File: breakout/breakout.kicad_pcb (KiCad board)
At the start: 2 copper layers, 20.3 x 22.9 mm, 6 parts, among them J1 Conn_01x02, J2 Conn_01x04, J3 Conn_01x05, J4 Conn_01x05, J5 Conn_01x03, U1 74HC4051

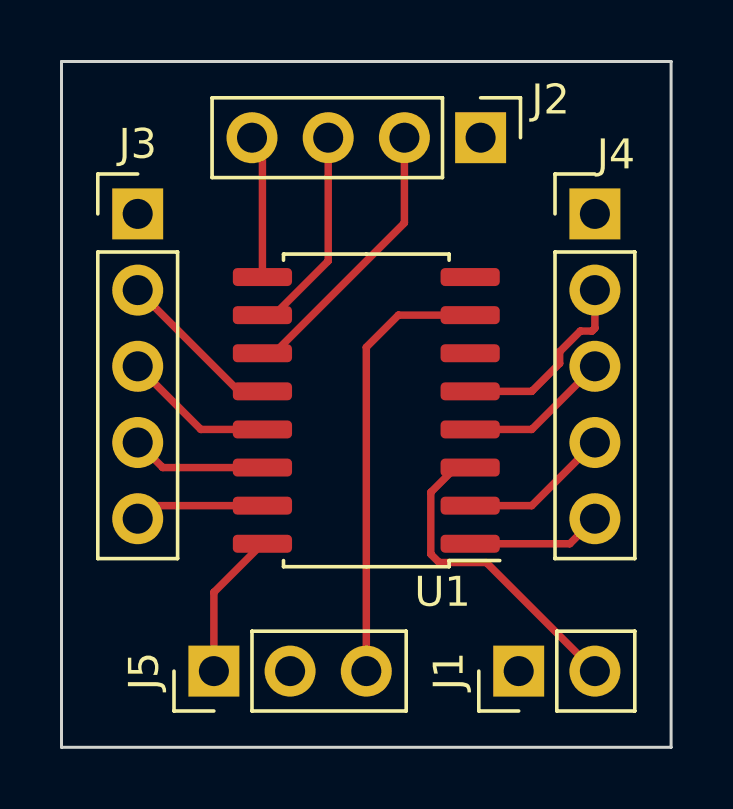
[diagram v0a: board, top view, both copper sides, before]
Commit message: Add 0805 decoupling capacitor pads to the breakout board.
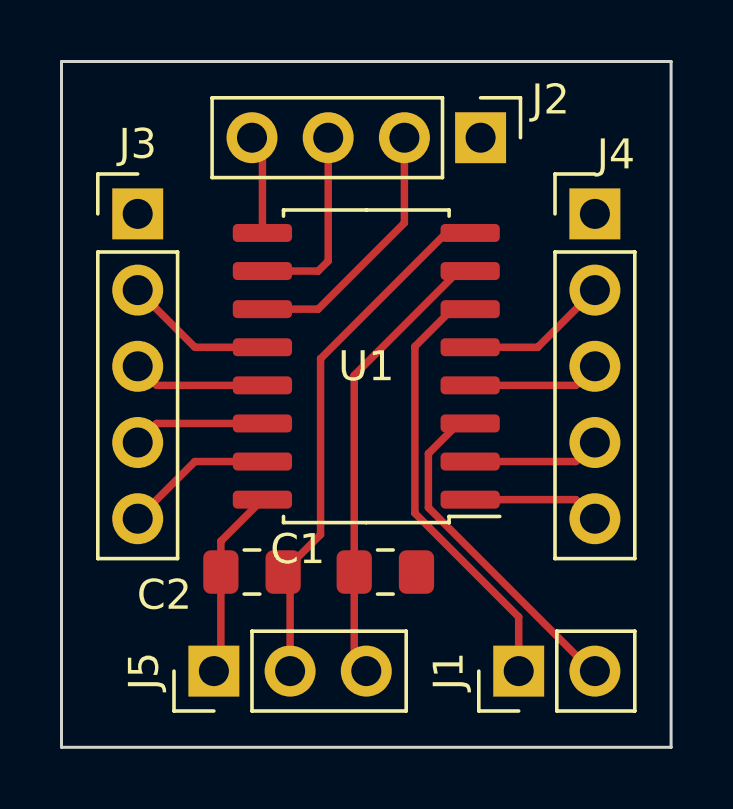
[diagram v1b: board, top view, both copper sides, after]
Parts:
- added C1: C, Capacitor_SMD:C_0805_2012Metric_Pad1.18x1.45mm_HandSolder, F.Cu at (130.2, 95.8)
- added C2: C, Capacitor_SMD:C_0805_2012Metric_Pad1.18x1.45mm_HandSolder, F.Cu at (125.7, 95.8)
- moved U1 1.47 mm to (129.5, 88.9)
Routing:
- net GND: track 0.00 -> 32.4 mm
- net Net-(J4-Pad2): track 6.53 -> 4.95 mm
- net VCC: track 4.91 -> 6.38 mm
- net Net-(J2-Pad4): track 4.79 -> 3.32 mm
- net VEE: track 14.7 -> 15.3 mm
- net Net-(J1-Pad2): track 10.8 -> 11.4 mm
- net Net-(J4-Pad4): track 5.03 -> 4.42 mm
- net Net-(J4-Pad3): track 5.03 -> 4.42 mm
- net Net-(J3-Pad5): track 4.34 -> 4.95 mm
- net Net-(J3-Pad3): track 5.03 -> 4.42 mm
- net Net-(J3-Pad2): track 5.56 -> 4.95 mm
- net Net-(J2-Pad3): track 7.05 -> 6.44 mm
- net Net-(J2-Pad2): track 9.37 -> 8.76 mm
